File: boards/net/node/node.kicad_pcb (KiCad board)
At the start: 4 copper layers, 48 x 48 mm, 60 parts, among them J1 N, J2 E, J3 S, J4 W, J5 SENSOR, J6 PROG, SW1 SW-18010P, U1 RP2040, U2 W25Q16JVSSIQ, U3 VL53L0CXV0DH/1, U4 ME6211C33M5G, Y1 12MHz

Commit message: net/node: LCSC numbers for every BOM line; crystal to ABM8-272-T3 with 15 pF
Every assembled line now has a verified JLCPCB part (make parts --boards
30: 0 errors, 0 warnings; 10 basic, 1 preferred, 9 extended). Passives
come from a PASSIVES table in schematic.py; descriptions carry the
real ratings.

- Y1: YXC X322512MSB4SI (C9002) is a 20 pF / 80 ohm part, not the 10 pF
  the design assumed. Switched to the RP2040 HDG crystal, Abracon
  ABM8-272-T3 (C20625731), with C1/C2 27 pF -> 15 pF C0G (C1644).
- D2/D4: WS2812B-2020 C965555 is discontinued; WS2812B-2020-V6
  (C52917434), same pinout.
- J1-J4: C144394 (3-pin B3B-XH-A; C144395 is the 4-pin B4B).
- J5 C32713273, U3 C91199, BZ1 C910763, D1 C81598, SW1 C2681585.

Regenerated node.kicad_sch/node.kicad_pcb: only fields, values and
descriptions differ (UUID-normalised); geometry, nets and fills are
unchanged. make check: 0 violations, 0 unconnected, 0 parity.

Co-Authored-By: Claude Opus 5.5 <noreply@anthropic.com>
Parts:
- C1, C2: value 27p -> 15p
- D2, D4: value WS2812B-2020 -> WS2812B-2020-V6

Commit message: net/node: side-entry JST S3B-XH-A link connectors, board re-placed
J1..J4 are now side-entry S3B-XH-A(LF)(SN) (C157928) on the middle of
each edge, mouths 1.1 mm past the edge, so cables leave in the board
plane and a node lies flat. Pinout per connector unchanged (1 = +5V,
2 = DATA, 3 = GND; straight cables); pin 1 is now the counter-clockwise
first pin on each edge. J4 sits 4.9 mm south of centre (U1's cap
column). Footprint: repo copy of the stock one with silk trimmed off
the board edge (pads, courtyard, fab and 3D identical).

J5, J6, BZ1, link resistors and some plane caps moved; the earlier
review fixes (C11, crystal loop, USB series R, pogo paste) are intact.
make check: 0 violations, 0 unconnected, 0 parity. LED note now quotes
the V6's VIH = 0.55 VDD. Order unpanelised (overhang).

Co-Authored-By: Claude Opus 5.5 <noreply@anthropic.com>
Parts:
- J1, J2, J3, J4: footprint Connector_JST:JST_XH_B3B-XH-A_1x03_P2.50mm_Vertical -> boards:JST_XH_S3B-XH-A_1x03_P2.50mm_Horizontal_EdgeMount
- moved J5 25.7 mm to (96.4, 88.8), turned to -90 degrees
- moved C16 13.7 mm to (70.0, 85.2), turned to 0 degrees
- moved C3 11.2 mm to (83.0, 67.5)
- moved C5 11.2 mm to (81.0, 64.3), turned to 0 degrees
- moved C8 9.53 mm to (81.0, 62.5), turned to 0 degrees
- moved BZ1 7.86 mm to (91.8, 63.4), turned to 0 degrees
- moved J3 6.87 mm to (71.4, 89.9), turned to 0 degrees
- moved J1 6.79 mm to (76.5, 58.1), turned to 180 degrees
- moved J2 6.79 mm to (89.9, 76.5), turned to 90 degrees
- moved R13 4.95 mm to (61.8, 78.4)
- moved R14 4.82 mm to (61.8, 81.4)
- moved J4 4.60 mm to (58.1, 76.4), turned to -90 degrees
- moved R8 4.46 mm to (72.5, 62.6), turned to -90 degrees
- moved R7 4.20 mm to (74.0, 62.6), turned to 90 degrees
- moved R10 3.50 mm to (85.5, 75.6)
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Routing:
- net Net-(BZ1--): track 4.43 -> 20.0 mm
- net /SDA: track 41.5 -> 52.9 mm
- net +5V: track 202.0 -> 213.1 mm, vias 2 -> 5
- net Net-(BZ1-+): track 17.0 -> 7.82 mm
- net Net-(J3-Pin_2): track 11.2 -> 4.59 mm
- net +3V3: track 52.4 -> 47.4 mm, vias 26 -> 24
- net /LINK_N: track 21.8 -> 17.5 mm
- net Net-(J1-Pin_2): track 7.25 -> 3.50 mm
- net Net-(J6-Pin_3): track 15.4 -> 18.7 mm
- net /SCL: track 45.2 -> 48.4 mm, vias 1 -> 0
- net /LINK_E: track 38.6 -> 35.9 mm
- net /SENS_INT: track 55.2 -> 57.9 mm, vias 3 -> 2
- net /RUN: track 38.7 -> 41.1 mm
- net /QSPI_SS: track 28.5 -> 30.8 mm
- net Net-(J6-Pin_1): track 19.5 -> 21.8 mm
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
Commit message: net/node: link connectors centred and aligned for tiling; U1 caps to 0402
J1..J4 now sit with pin 2 exactly on each edge's centre line (24.0 on
the 48 x 48 board), so a node's W/S connectors line up with its
neighbours' E/N connectors when the net is tiled by translation.
pcb.py derives the rows from the board centre and refuses to generate
a board whose facing rows are misaligned or off-centre.

To free the west edge for J4, the U1 decoupling caps C10/C15 (100 nF,
C307331) and C11/C13 (1 uF, C52923) are now 0402, packed beside pins
43-45: pin-to-cap tracks went from 2.6-8.0 mm to 1.4-2.9 mm. C9 moved
0.5 mm and DM/DP re-routed; R15/R16, the crystal, pogo pads and M2
holes are unchanged. J5 moved 0.07 mm east to clear J3's courtyard,
leaving two silk_edge_clearance warnings (documented).

README: tiling rule and half-twist cable note, 0402 decision, variant
BOM command groups like the jobset so 0402/0603 parts stay separate.

Co-Authored-By: Claude Opus 5.5 <noreply@anthropic.com>
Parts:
- C10, C11, C13, C15: footprint Capacitor_SMD:C_0603_1608Metric -> Capacitor_SMD:C_0402_1005Metric
- moved J4 4.90 mm to (58.1, 71.5)
- moved C15 4.72 mm to (61.8, 69.0), turned to -90 degrees
- moved C13 4.23 mm to (61.3, 67.6)
- moved C11 2.70 mm to (59.0, 66.8)
- moved C9 0.50 mm to (63.9, 70.7)
- moved J3 0.10 mm to (71.5, 89.9)
- moved C10 0.08 mm to (59.0, 67.8)
- moved J5 0.07 mm to (96.5, 88.8)
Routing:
- net /DVDD: track 40.1 -> 28.0 mm
- net GND: track 36.5 -> 37.9 mm, vias 33 -> 32

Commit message: net/node: re-floorplan (MCU centre, peripherals in corners); J5 removed
U1 (rotated 180) and its support (decoupling, crystal, flash, LDO,
USB series R) now fill the centre between the four edge-centred link
connectors; peripherals take the corners: BZ1 NE, VL53L0X SE, pogo
pads J6 SW, SW1 NW. LED D2 sits just NE of U1. The 5 V ring is closed.

J5 (1x7 sensor header) is removed: its courtyard fits no corner and it
carried the longest run (SENS_AIN). GPIO26 is a no-connect; the bare
variant is now a sensorless relay node.

Mounting holes: no pad, via or footprint within 3.7 mm of a hole
centre (C2 had been 3.08 mm from H1; an M2 washer is 5 mm OD),
enforced by annulus keepouts (pcbgen.keepout r_in/pads/footprints/
tracks) and a pcb.py assertion. Crystal copper 23.3 -> 16.2 mm, USB
pair ~26 -> ~23 mm; make check: 0 violations, 0 warnings.

Co-Authored-By: Claude Opus 5.5 <noreply@anthropic.com>
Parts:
- removed J5: SENSOR, Connector_PinHeader_2.54mm:PinHeader_1x07_P2.54mm_Vertical
- moved SW1 40.5 mm to (61.0, 57.5)
- moved C22 34.6 mm to (65.5, 57.5), turned to 90 degrees
- moved C12 26.9 mm to (65.5, 66.2), turned to 0 degrees
- moved R4 25.6 mm to (93.3, 80.9), turned to 0 degrees
- moved C2 23.3 mm to (78.0, 62.9), turned to 180 degrees
- moved C18 21.7 mm to (68.4, 63.5), turned to -90 degrees
- moved U4 20.9 mm to (65.5, 63.5)
- moved C17 20.6 mm to (62.2, 63.5)
- moved C8 20.6 mm to (75.4, 82.3), turned to -90 degrees
- moved U2 20.0 mm to (84.6, 83.5), turned to 180 degrees
- moved R1 19.6 mm to (75.0, 63.0), turned to 180 degrees
- moved C1 18.1 mm to (79.4, 67.0), turned to 180 degrees
- moved R5 17.9 mm to (96.3, 80.9), turned to 180 degrees
- moved Y1 17.6 mm to (76.1, 65.9)
- moved C14 17.4 mm to (70.7, 67.6)
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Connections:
- U1 pad 38: /SENS_AIN -> unconnected-(U1-GPIO26/ADC0-Pad38)
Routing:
- net /SENS_AIN: track 61.6 -> 0.00 mm, vias 1 -> 0
- net /LINK_E: track 35.9 -> 7.82 mm, vias 2 -> 0
- net /SDA: track 53.0 -> 27.5 mm, vias 1 -> 2
- net +5V: track 213.1 -> 234.3 mm, vias 5 -> 1
- net /SCL: track 48.5 -> 29.3 mm, vias 0 -> 2
- net /QSPI_SS: track 30.8 -> 47.9 mm, vias 0 -> 3
- net Net-(BZ1--): track 20.0 -> 5.70 mm
- net /SWCLK: track 44.1 -> 32.6 mm
- net /RUN: track 41.1 -> 29.8 mm
- net /SENS_INT: track 57.8 -> 69.1 mm, vias 2 -> 3
- net /LINK_W: track 30.9 -> 19.8 mm
- net /SWDIO: track 40.5 -> 31.8 mm
- net Net-(J1-Pin_2): track 3.50 -> 9.39 mm, vias 1 -> 0
- net /LINK_N: track 17.5 -> 22.8 mm
- net Net-(C2-Pad2): track 7.81 -> 3.33 mm
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
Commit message: net/node: isolate the crystal (buzzer to GPIO18/19, guard pour, 1 mm rule); J6 centred
The piezo drive moved from GPIO12/13 (pins 15/16, four pins from
XIN/XOUT) to GPIO18/19 (PWM slice 1 A/B, pins 29/30), routed on B.Cu
under U1 to BZ1; BUZZ_B went from 0.55 to 2.0 mm from crystal copper.

Every other non-GND net now keeps >= 1.0 mm (same layer, edge to edge)
from the crystal nets and the LED nets and all D4 pads >= 2.0 mm,
checked by generate/xtal_check.py (tracks, arcs with sagitta margin,
vias, pads, zones; rejects unmodelled copper) and asserted from
pcb.py. Known exemption: the IOVDD/DVDD escapes inside U1's pin field.
A notched F.Cu GND guard pour surrounds Y1/C1/C2/R1, stitched to In1
by 19 vias, asserted free of foreign copper. C19 now sits at D2's VDD
pin (LED loop 15.5 -> 8.7 mm).

J6 pogo pads centred in the SW corner (margins to J3/J4/H3 ring
0.57/0.58/0.60 mm); USB pair 22.0/19.8 mm; README jig coordinates
updated. make check: 0 violations, 0 warnings.

Co-Authored-By: Claude Opus 5.5 <noreply@anthropic.com>
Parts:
- moved J6 4.43 mm to (62.4, 85.9)
- moved R17 3.40 mm to (88.0, 67.7)
- moved R18 3.40 mm to (91.4, 67.7)
- moved C19 2.49 mm to (84.8, 61.8), turned to 0 degrees
- moved C1 1.17 mm to (80.0, 68.0)
- moved R1 0.77 mm to (75.8, 63.0)
- moved Y1 0.66 mm to (76.8, 66.0)
- moved D4 0.60 mm to (81.4, 64.2)
- moved D2 0.60 mm to (84.0, 64.2)
- moved R8 0.55 mm to (81.2, 59.0)
- moved C2 0.50 mm to (78.0, 62.4), turned to 90 degrees
- turned BZ1 to 0 degrees
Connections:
- U1 pad 15: /BUZZ_A -> unconnected-(U1-GPIO12-Pad15)
- U1 pad 16: /BUZZ_B -> unconnected-(U1-GPIO13-Pad16)
- U1 pad 29: unconnected-(U1-GPIO18-Pad29) -> /BUZZ_A
- U1 pad 30: unconnected-(U1-GPIO19-Pad30) -> /BUZZ_B
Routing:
- net /BUZZ_B: track 13.0 -> 24.8 mm, vias 0 -> 2
- net /BUZZ_A: track 15.9 -> 21.6 mm, vias 0 -> 2
- net /SWCLK: track 32.6 -> 28.0 mm
- net /RUN: track 29.8 -> 25.1 mm
- net +5V: track 234.3 -> 238.7 mm
- net /SWDIO: track 31.8 -> 27.6 mm
- net Net-(BZ1--): track 5.70 -> 9.81 mm
- net Net-(BZ1-+): track 9.81 -> 5.70 mm
- net Net-(J6-Pin_3): track 15.7 -> 12.5 mm
- net /QSPI_SS: track 47.9 -> 49.7 mm
- net GND: track 42.3 -> 40.5 mm, vias 29 -> 45
- net Net-(J6-Pin_1): track 18.1 -> 16.5 mm
- net Net-(J1-Pin_2): track 9.39 -> 8.20 mm
- net Net-(U1-XIN): track 5.77 -> 6.74 mm
- net Net-(C2-Pad2): track 3.33 -> 4.01 mm
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- added copper zone on F.Cu, net GND

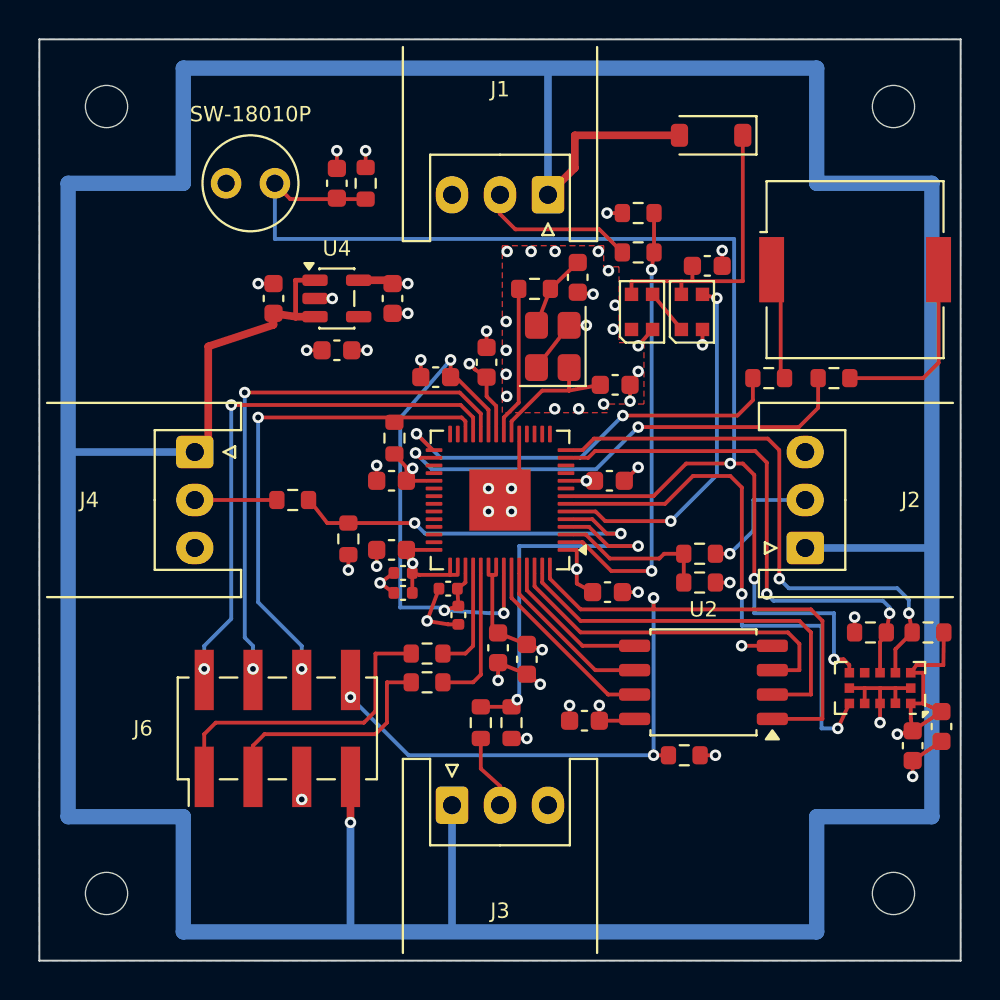
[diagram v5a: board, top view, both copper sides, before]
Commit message: net/node: four corner LEDs; pre-order panel fixes (BOOT 1k, TVS, USB Schottky)
Four WS2812B-2020-V6 (D1..D4, C52917434), one per corner, 4.0 mm in
from an edge and 8.8 mm from the corner, chained NE->NW->SW->SE on
GPIO4, so a node shows the direction a pattern moves (2x2 sub-pixels).
Each has its own 100 nF 0402. The LEDs run from +5V through
U5 SN74AHCT1G125 (C7484) as level shifter; the 1N4148W drop diode is
gone (at LED idle current it no longer guaranteed VIH). Board stays
48 x 48; budget ~215 mA/node full white.

Fixes from the cross-model pre-order review:
- R19 1 k between QSPI_SS and the BOOT pogo pad, at the flash (RP2040
  hardware design guide p.9); J6.8 no longer shorts QSPI_SS.
- D5 SMF5.0A TVS on +5V at the LDO input (energy sink; limits
  documented, measure the plug transient on first boards).
- D6 B5819W from the jig's USB 5 V to +5V, so a powered net cannot
  backfeed the host.
- J1-J4 and SW1 out of the position files (hand-soldered);
  pcbgen carries base exclusions into variants (+ test).
- J6 vias moved out of the pogo pads; piezo drive modes without DC.

make check: 0 violations, 0 warnings; make parts --boards 30 clean.

Co-Authored-By: Claude Opus 5.5 <noreply@anthropic.com>
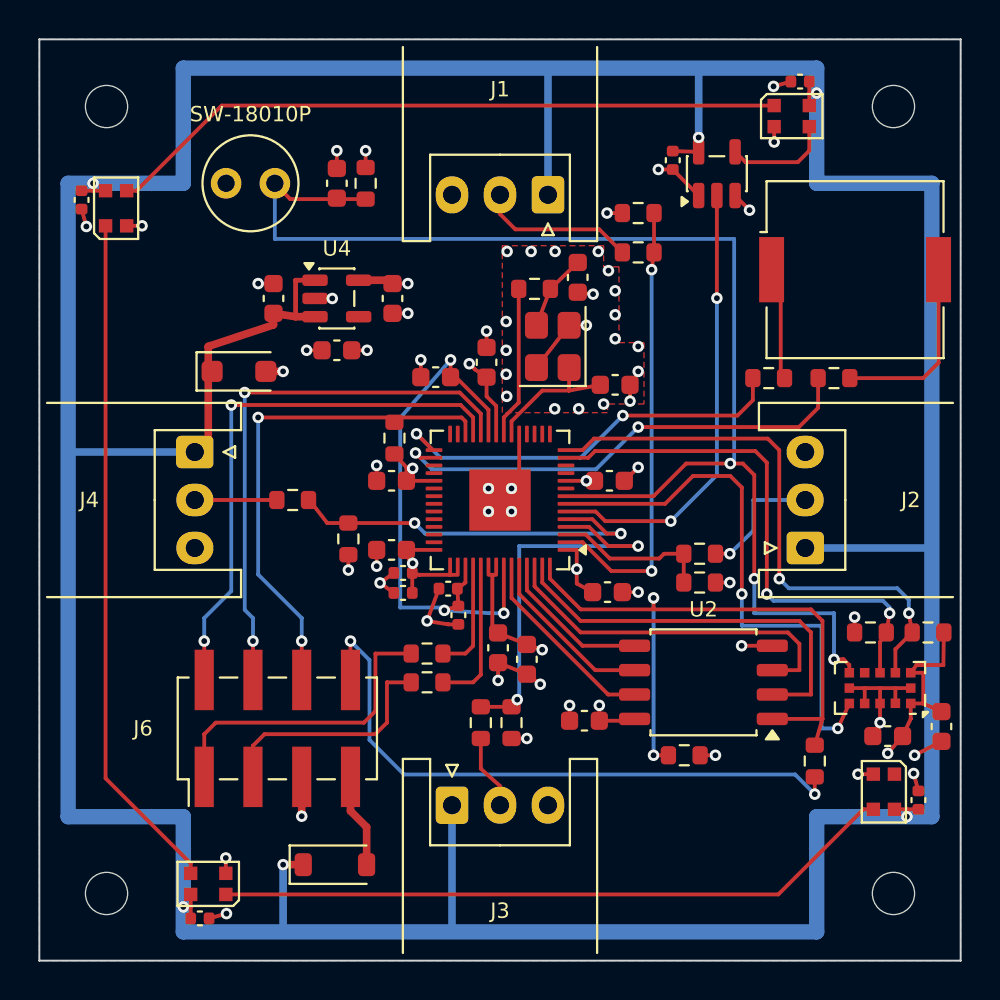
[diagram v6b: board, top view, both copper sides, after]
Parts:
- added C23: 100n, Capacitor_SMD:C_0402_1005Metric, F.Cu at (52.2, 58.4)
- added C24: 100n, Capacitor_SMD:C_0402_1005Metric, F.Cu at (58.4, 95.8)
- added C25: 100n, Capacitor_SMD:C_0402_1005Metric, F.Cu at (95.8, 89.6)
- added C26: 100n, Capacitor_SMD:C_0402_1005Metric, F.Cu at (83.0, 56.3)
- added D3: WS2812B-2020-V6, LED_SMD:LED_WS2812B-2020_PLCC4_2.0x2.0mm, F.Cu at (58.8, 94.0)
- added D5: SMF5.0A, Diode_SMD:D_SOD-123F, F.Cu at (60.4, 67.3)
- added D6: B5819W, Diode_SMD:D_SOD-123, F.Cu at (65.4, 93.0)
- added R19: 1k, Resistor_SMD:R_0603_1608Metric, F.Cu at (90.4, 87.6)
- added U5: 74AHCT1G125, Package_TO_SOT_SMD:SOT-23-5, F.Cu at (85.3, 57.0)
- C19: footprint Capacitor_SMD:C_0603_1608Metric -> Capacitor_SMD:C_0402_1005Metric
- D1: value 1N4148W -> WS2812B-2020-V6; footprint Diode_SMD:D_SOD-123 -> LED_SMD:LED_WS2812B-2020_PLCC4_2.0x2.0mm
- moved D2 30.5 mm to (54.0, 58.8)
- moved D4 28.0 mm to (94.0, 89.2), turned to -90 degrees
- moved C19 10.7 mm to (89.6, 52.2), turned to 180 degrees
- moved D1 4.32 mm to (89.2, 54.0), turned to 0 degrees
- moved C21 1.39 mm to (94.2, 86.3), turned to 180 degrees
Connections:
- C19 pad 1: /LED_VDD -> +5V
- D1 pad 1: /LED_VDD -> /LED_CH1
- D1 pad 2: +5V -> GND
- D2 pad 1: Net-(D2-DOUT) -> /LED_CH2
- D2 pad 3: /LED_DIN -> /LED_CH1
- D2 pad 4: /LED_VDD -> +5V
- D4 pad 3: Net-(D2-DOUT) -> /LED_CH3
- D4 pad 4: /LED_VDD -> +5V
- J6 pad 7: +5V -> Net-(D6-A)
- J6 pad 8: /QSPI_SS -> /BOOT
- U1 pad 6: /LED_DIN -> /LED_DATA
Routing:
- net /LED_CH3: track 0.00 -> 35.6 mm
- net /LED_CH2: track 0.00 -> 35.6 mm
- net /LED_CH1: track 0.00 -> 35.6 mm
- net /BOOT: track 0.00 -> 32.9 mm, vias 0 -> 2
- net /LED_DATA: track 0.00 -> 23.2 mm, vias 0 -> 2
- net /QSPI_SS: track 49.7 -> 34.1 mm, vias 3 -> 2
- net /LED_VDD: track 15.6 -> 0.00 mm
- net /LED_DIN: track 18.6 -> 5.58 mm, vias 2 -> 0
- net GND: track 40.5 -> 50.0 mm, vias 45 -> 55
- net Net-(D6-A): track 0.00 -> 4.92 mm
- net Net-(D2-DOUT): track 2.37 -> 0.00 mm
- net +3V3: track 46.2 -> 45.2 mm
- net /SWCLK: track 28.0 -> 28.5 mm
- net /SWDIO: track 27.6 -> 28.2 mm
- net /RUN: track 25.1 -> 25.7 mm
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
